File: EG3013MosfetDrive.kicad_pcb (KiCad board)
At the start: 2 copper layers, 38 x 29.8 mm, 35 parts, among them J1 Conn_02x03_Odd_Even, Q1 QM6006D, Q2 QM6006D, Q3 QM6006D, Q4 QM6006D, U1 EG3013, U2 EG3013

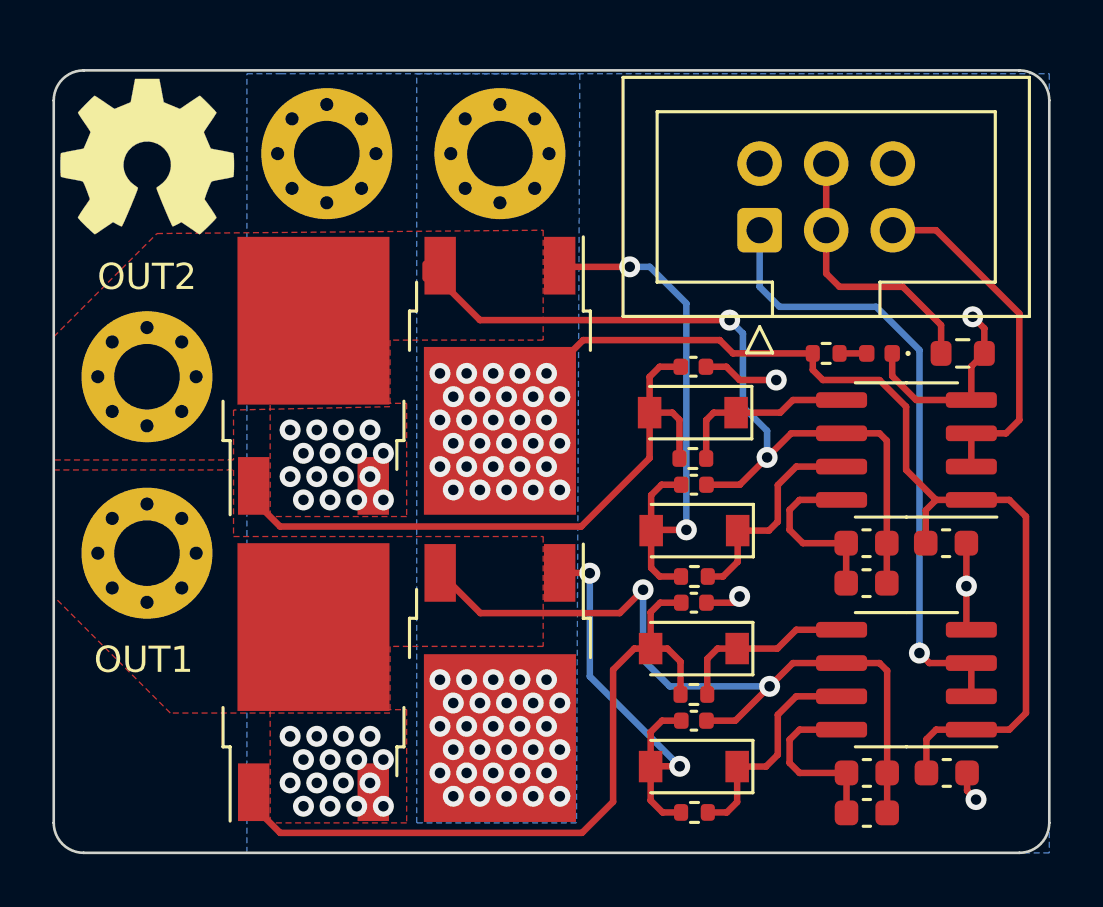
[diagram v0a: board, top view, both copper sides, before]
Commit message: PWM端口添加下拉电阻
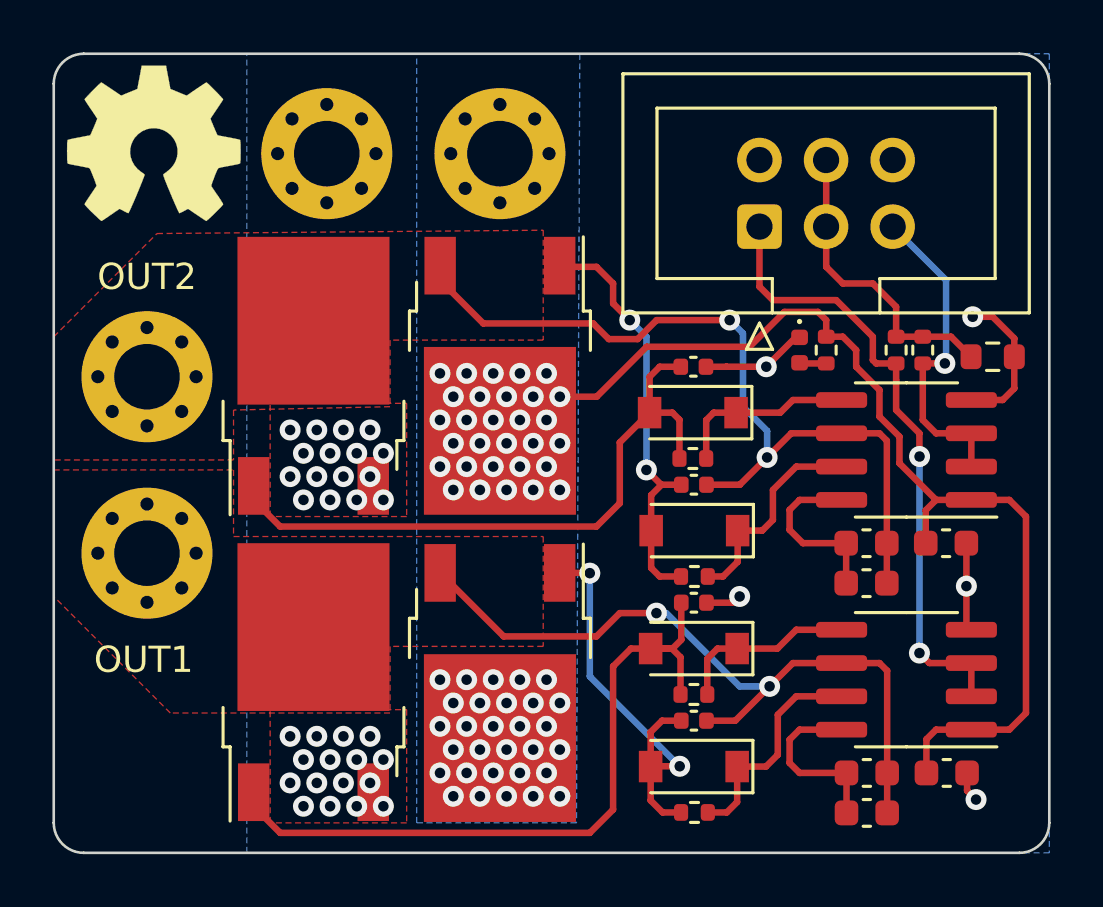
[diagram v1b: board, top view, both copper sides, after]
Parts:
- removed the REF** at (117.3, 89.3)
- added R7: 1k, Resistor_SMD:R_0402_1005Metric, F.Cu at (136.8, 93.0)
- added R8: 1k, Resistor_SMD:R_0402_1005Metric, F.Cu at (135.8, 93.0)
- moved D5 3.05 mm to (132.1, 93.0), turned to -90 degrees
- moved REF** 1.52 mm to (125.5, 96.1)
- moved R6 1.15 mm to (139.4, 93.2)
- moved REF** 0.57 mm to (107.4, 85.1)
- moved J1 0.14 mm to (130.6, 88.3)
- moved R5 0.13 mm to (133.1, 93.0), turned to -90 degrees
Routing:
- net Net-(C3-Pad2): track 20.8 -> 16.1 mm
- net +12V: track 41.7 -> 40.0 mm
- net OUT1: track 30.0 -> 28.4 mm
- net GND: track 10.5 -> 11.9 mm
- net IN2: track 13.5 -> 12.4 mm, vias 0 -> 1
- net GNDPWR: track 16.6 -> 15.6 mm
- net OUT2: track 31.3 -> 31.9 mm
- net IN1: track 24.2 -> 24.1 mm, vias 1 -> 2
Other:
- board size 38 x 29.8 mm -> 38 x 30.5 mm
- board text added: "Designed by zenchrer with Kicad"
- board text removed: "+"
- board text removed: "-"

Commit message: fix some net
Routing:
- net IN1: track 24.1 -> 22.7 mm
- net OUT2: track 31.9 -> 31.0 mm
- net +12V: track 40.0 -> 39.4 mm

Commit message: model D Vesion
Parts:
- removed the REF** at (107.4, 85.1)
- added C11: 100nF, Capacitor_SMD:C_0603_1608Metric, F.Cu at (149.3, 80.1)
- added C12: 100nF, Capacitor_SMD:C_0603_1608Metric, F.Cu at (149.3, 102.6)
- added C13: 10nF, Capacitor_SMD:C_0402_1005Metric, F.Cu at (137.8, 81.5)
- added C14: 10nF, Capacitor_SMD:C_0402_1005Metric, F.Cu at (137.7, 87.7)
- added C15: 10nF, Capacitor_SMD:C_0402_1005Metric, F.Cu at (137.7, 104.0)
- added C16: 10nF, Capacitor_SMD:C_0402_1005Metric, F.Cu at (137.7, 110.2)
- added C17: 22uF, Capacitor_SMD:C_0603_1608Metric, F.Cu at (144.2, 87.0)
- added C18: 22uF, Capacitor_SMD:C_0603_1608Metric, F.Cu at (142.5, 109.5)
- added C19: 22uF, Capacitor_SMD:C_0603_1608Metric, F.Cu at (142.5, 87.0)
- added C20: 22uF, Capacitor_SMD:C_0603_1608Metric, F.Cu at (144.2, 109.5)
- added D6: 1N4148, Diode_SMD:D_SOD-123, F.Cu at (138.9, 83.4)
- added D7: 1N4148, Diode_SMD:D_SOD-123, F.Cu at (138.9, 85.9)
- added D8: 1N4148, Diode_SMD:D_SOD-123, F.Cu at (138.9, 105.9)
- added D9: 1N4148, Diode_SMD:D_SOD-123, F.Cu at (138.9, 108.4)
- added H5: Pad, MountingHole:MountingHole_2.5mm_Pad_Via, F.Cu at (116.6, 81.8)
- added H6: Pad, MountingHole:MountingHole_2.5mm_Pad_Via, F.Cu at (116.6, 104.1)
- added Q5: QM6006D, Package_TO_SOT_SMD:TO-252-2, F.Cu at (131.3, 85.8)
- added Q6: QM6006D, Package_TO_SOT_SMD:TO-252-2, F.Cu at (124.2, 85.8)
- added Q7: QM6006D, Package_TO_SOT_SMD:TO-252-2, F.Cu at (131.3, 108.2)
- added Q8: QM6006D, Package_TO_SOT_SMD:TO-252-2, F.Cu at (124.2, 108.2)
- added R10: 1k, Resistor_SMD:R_0402_1005Metric, F.Cu at (139.9, 112.0)
- added R11: 22R, Resistor_SMD:R_0402_1005Metric, F.Cu at (140.0, 81.5)
- added R12: 22R, Resistor_SMD:R_0402_1005Metric, F.Cu at (140.0, 87.7)
- added R13: 22R, Resistor_SMD:R_0402_1005Metric, F.Cu at (140.0, 104.0)
- added R14: 22R, Resistor_SMD:R_0402_1005Metric, F.Cu at (140.0, 110.2)
- added R9: 1k, Resistor_SMD:R_0402_1005Metric, F.Cu at (142.0, 112.0)
- added REF**: Symbol_Barrel_Polarity, Symbol:Symbol_Barrel_Polarity, F.Cu at (125.3, 123.3)
- added REF**: Symbol_Barrel_Polarity, Symbol:Symbol_Barrel_Polarity, B.Cu at (125.3, 123.4)
- added REF**: OSHW-Symbol_8.9x8mm_SilkScreen, Symbol:OSHW-Symbol_8.9x8mm_SilkScreen, B.Cu at (143.4, 73.8)
- added U3: EG3013, Package_SO:SOIC-8_3.9x4.9mm_P1.27mm, F.Cu at (148.1, 84.8)
- added U4: EG3013, Package_SO:SOIC-8_3.9x4.9mm_P1.27mm, F.Cu at (148.1, 107.2)
- C1, C2: value 10nF -> 100nF; footprint Capacitor_SMD:C_0402_1005Metric -> Capacitor_SMD:C_0603_1608Metric
- C10, C9: value 100nF -> 22uF
- C5, C6: value 22uF -> 10nF; footprint Capacitor_SMD:C_0603_1608Metric -> Capacitor_SMD:C_0402_1005Metric
- D1: value 1N4148 -> LED_Small; footprint Diode_SMD:D_SOD-123 -> LED_SMD:LED_0402_1005Metric
- D5: value LED_Small -> 1N4148; footprint LED_SMD:LED_0402_1005Metric -> Diode_SMD:D_SOD-123
- R1: value 22R -> 0R; footprint Resistor_SMD:R_0402_1005Metric -> Resistor_SMD:R_0603_1608Metric
- R2: value 22R -> 4.7k
- R5: value 4.7k -> 22R
- R6: value 0R -> 22R; footprint Resistor_SMD:R_0603_1608Metric -> Resistor_SMD:R_0402_1005Metric
- moved C2 39.8 mm to (149.3, 69.0)
- moved C7 34.7 mm to (144.2, 75.7), turned to 90 degrees
- moved H1 34.7 mm to (121.5, 119.4), turned to -90 degrees
- moved U1 34.2 mm to (148.1, 73.5), turned to -90 degrees
- moved D2 33.9 mm to (138.9, 72.2)
- moved H4 33.6 mm to (129.1, 119.4), turned to -90 degrees
- moved R3 33.5 mm to (140.0, 70.3)
- moved J1 33.2 mm to (145.4, 118.0), turned to -90 degrees
- moved Q1 32.9 mm to (131.3, 74.6)
- moved Q2 32.8 mm to (124.2, 74.6)
- moved C3 29.4 mm to (137.7, 70.3), turned to 0 degrees
- moved D3 27.3 mm to (138.9, 74.7)
- moved C1 26.4 mm to (149.3, 91.4)
- moved C9 25.1 mm to (142.5, 75.7), turned to 90 degrees
- moved R4 23.7 mm to (140.0, 76.7)
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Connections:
- C1 pad 1: OUT1 -> +12V
- C1 pad 2: Net-(C1-Pad2) -> GNDPWR
- C10 pad 1: +12V -> Net-(C10-Pad1)
- C10 pad 2: GNDPWR -> OUT3
- C2 pad 1: GNDPWR -> +12V
- C2 pad 2: Net-(C2-Pad2) -> GNDPWR
- C3 pad 1: OUT2 -> OUT1
- C5 pad 1: Net-(C5-Pad1) -> OUT3
- C5 pad 2: OUT1 -> Net-(C5-Pad2)
- C6 pad 1: Net-(C6-Pad1) -> GNDPWR
- C6 pad 2: OUT2 -> Net-(C6-Pad2)
- C7 pad 1: Net-(C5-Pad1) -> Net-(C7-Pad1)
- C8 pad 1: Net-(C6-Pad1) -> Net-(C10-Pad1)
- C8 pad 2: OUT2 -> OUT3
- C9 pad 1: +12V -> Net-(C7-Pad1)
- C9 pad 2: GNDPWR -> OUT1
- D1 pad 1: Net-(D1-Pad1) -> GNDPWR
- D1 pad 2: Net-(C1-Pad2) -> Net-(D1-Pad2)
- D2 pad 2: Net-(C2-Pad2) -> Net-(C3-Pad2)
- D3 pad 2: Net-(C3-Pad2) -> Net-(C4-Pad2)
- D4 pad 2: Net-(C4-Pad2) -> Net-(C5-Pad2)
- D5 pad 1: GNDPWR -> Net-(D5-Pad1)
- D5 pad 2: Net-(D5-Pad2) -> Net-(C6-Pad2)
- H2 pad 1: +12V -> OUT1
- H3 pad 1: OUT1 -> OUT3
- H4 pad 1: OUT2 -> +12V
- J1 pad 2: unconnected-(J1-Pad2) -> IN3
- J1 pad 6: unconnected-(J1-Pad6) -> IN4
- Q1 pad 1: Net-(C1-Pad2) -> Net-(C3-Pad2)
- Q2 pad 1: Net-(C2-Pad2) -> Net-(C4-Pad2)
- Q3 pad 1: Net-(C3-Pad2) -> Net-(C5-Pad2)
- Q3 pad 3: OUT2 -> OUT3
- Q4 pad 1: Net-(C4-Pad2) -> Net-(C6-Pad2)
- Q4 pad 2: OUT2 -> OUT3
- R1 pad 1: Net-(C1-Pad2) -> GNDPWR
- R1 pad 2: Net-(D1-Pad1) -> GND
- R2 pad 1: Net-(C2-Pad2) -> +12V
- R2 pad 2: Net-(D2-Pad1) -> Net-(D1-Pad2)
- R3 pad 2: Net-(D3-Pad1) -> Net-(D2-Pad1)
- R4 pad 2: Net-(D4-Pad1) -> Net-(D3-Pad1)
- R5 pad 1: +12V -> Net-(C5-Pad2)
- R5 pad 2: Net-(D5-Pad2) -> Net-(D4-Pad1)
- R6 pad 1: GNDPWR -> Net-(C6-Pad2)
- R6 pad 2: GND -> Net-(D5-Pad1)
- U1 pad 5: Net-(D2-Pad1) -> Net-(D3-Pad1)
- U1 pad 7: Net-(D1-Pad1) -> Net-(D2-Pad1)
- U1 pad 8: Net-(C5-Pad1) -> Net-(C7-Pad1)
- U2 pad 2: IN2 -> IN3
- U2 pad 3: IN2 -> IN3
- U2 pad 5: Net-(D4-Pad1) -> Net-(D5-Pad1)
- U2 pad 6: OUT2 -> OUT3
- U2 pad 7: Net-(D3-Pad1) -> Net-(D4-Pad1)
- U2 pad 8: Net-(C6-Pad1) -> Net-(C10-Pad1)
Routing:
- net GNDPWR: track 15.4 -> 101.8 mm, vias 37 -> 56
- net +12V: track 39.4 -> 88.9 mm, vias 60 -> 157
- net IN3: track 0.00 -> 38.4 mm, vias 0 -> 1
- net IN1: track 22.7 -> 58.1 mm, vias 2 -> 0
- net IN2: track 12.2 -> 44.8 mm, vias 1 -> 2
- net Net-(C2-Pad2): track 28.0 -> 0.00 mm
- net OUT4: track 0.00 -> 26.6 mm
- net OUT3: track 0.00 -> 26.1 mm
- net IN4: track 0.00 -> 25.9 mm, vias 0 -> 2
- net Net-(C14-Pad2): track 0.00 -> 25.3 mm
- net Net-(C6-Pad2): track 0.00 -> 24.9 mm
- net Net-(C16-Pad2): track 0.00 -> 24.9 mm
- net Net-(C1-Pad2): track 16.2 -> 0.00 mm, vias 2 -> 0
- net Net-(D8-Pad1): track 0.00 -> 13.3 mm
- net Net-(D6-Pad1): track 0.00 -> 12.3 mm
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- added copper zone on F.Cu, net OUT3
- added copper zone on F.Cu, net OUT4
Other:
- board size 38 x 30.5 mm -> 40.6 x 57.1 mm
- board text added: "+"
- board text added: "-"
- board text added: "IN3"
- board text added: "IN4"
- board text added: "OUT3"
- board text added: "OUT4"
- board text removed: "Designed by zenchrer with Kicad"
- board text removed: "NC"
